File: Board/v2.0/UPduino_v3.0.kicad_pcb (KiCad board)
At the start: 4 copper layers, 62 x 22.2 mm, 116 parts, among them J1 47589-0001, J2 Right, J3 Left, J4 5V Power, U1 93LC56BT-I/OT, U2 ICE40UP5K-SG48ITR, U3 FT232H, U4 SG-210STF 12.0000ML3, U5 W25Q32JVSSIM, U6 AP2127K-3.3, U7 AP2127K-1.2, U8 SN74AUP2G125DCUR

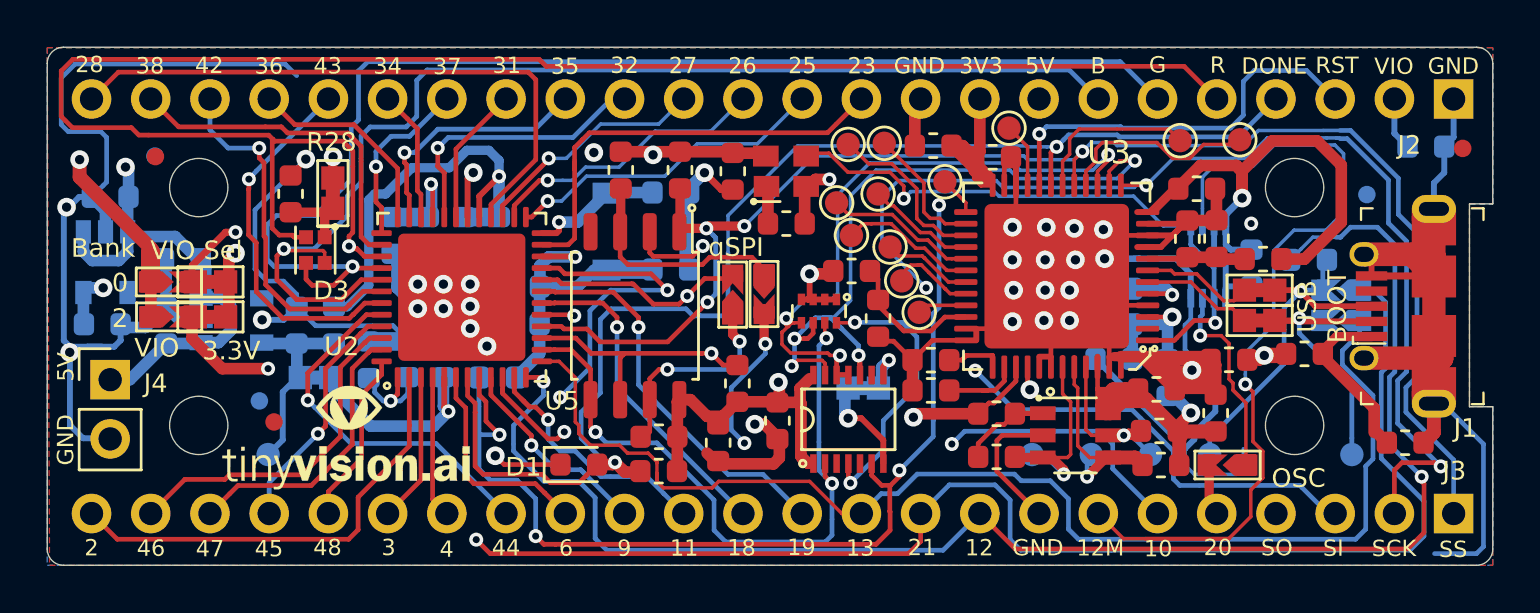
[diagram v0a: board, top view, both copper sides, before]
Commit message: Changed diode footprint, LED, modified FTDI reset, silkscreen for board and a few other changes
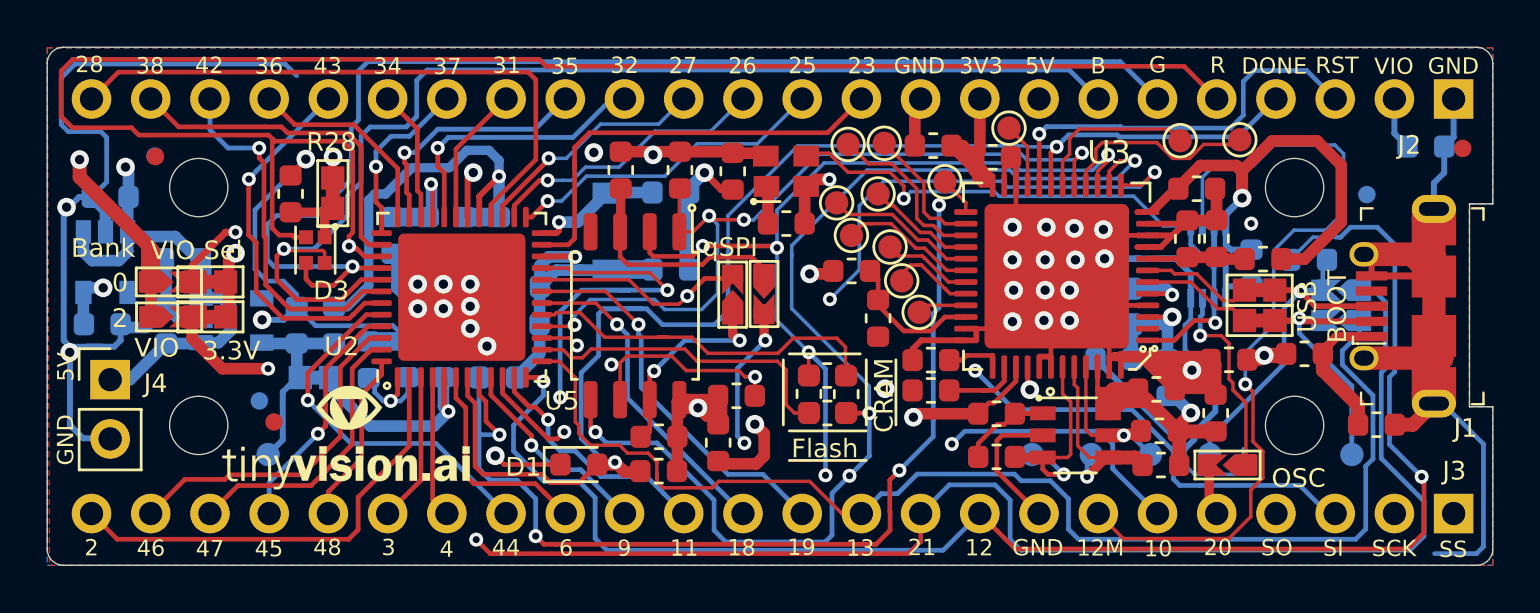
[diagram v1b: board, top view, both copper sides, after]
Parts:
- removed C32: 0.1u, Capacitor_SMD:C_0603_1608Metric
- removed RN1: YC124-JR-071KL, Resistor_SMD:R_Array_Concave_4x0402
- removed S1: TC7MPB9327FK(EL), vs:VSSOP14-P0.5-3X4
- added R11: DNI, Resistor_SMD:R_0603_1608Metric, F.Cu at (132.7, 92.7)
- added R12: 0, Resistor_SMD:R_0603_1608Metric, F.Cu at (133.5, 93.5)
- added R13: 0, Resistor_SMD:R_0603_1608Metric, F.Cu at (133.4, 91.9)
- D1: value HSMG-C120 -> LTST-C191KGKT
- R27: value JUMPER -> DNI; footprint vs:ShortedJumper-2_P1.3mm_Bridged_Pad1.0x1.0mm -> Resistor_SMD:R_0603_1608Metric; moved to F.Cu
- moved REF** 12.5 mm to (125.6, 92.5)
- moved REF** 9.26 mm to (136.5, 88.5)
- moved C25 1.45 mm to (157.0, 94.0)
- moved R27 0.77 mm to (134.3, 92.7), turned to 90 degrees
- moved R9 0.53 mm to (129.6, 92.7), turned to 180 degrees
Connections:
- R27 pad 1: GND -> /FLASH_MOSI
- R27 pad 2: Net-(R27-Pad2) -> /FPGA_SI
- R8 pad 1: /ICE_SS -> /FT_SSn
- R9 pad 1: /ICE_SCK -> /FT_SCK
- U2 pad 14: /FLASH_MOSI -> /FPGA_SO
- U2 pad 15: /ICE_SCK -> /FT_SCK
- U2 pad 16: /ICE_SS -> /FT_SSn
- U2 pad 17: /FLASH_MISO -> /FPGA_SI
- U3 pad 13: /ICE_SCK -> /FT_SCK
- U3 pad 14: /ICE_MOSI -> /FLASH_MOSI
- U3 pad 15: /ICE_MISO -> /FLASH_MISO
- U3 pad 17: /ICE_SS -> /FT_SSn
- U3 pad 39: +3V3 -> Net-(U3-Pad39)
- U5 pad 1: /ICE_SS -> /FT_SSn
- U5 pad 6: /ICE_SCK -> /FT_SCK
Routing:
- net /ICE_SCK: track 68.7 -> 0.00 mm, vias 4 -> 0
- net /ICE_SS: track 64.6 -> 0.00 mm, vias 4 -> 0
- net /FT_SCK: track 0.00 -> 36.9 mm, vias 0 -> 5
- net /FT_SSn: track 0.00 -> 34.6 mm, vias 0 -> 4
- net /ICE_MOSI: track 31.8 -> 0.00 mm, vias 4 -> 0
- net /ICE_MISO: track 28.8 -> 0.00 mm, vias 3 -> 0
- net /FLASH_MOSI: track 56.5 -> 72.8 mm, vias 4 -> 5
- net /FPGA_SI: track 0.00 -> 15.9 mm
- net +3V3: track 135.8 -> 120.2 mm
- net /FPGA_SO: track 0.00 -> 13.8 mm
- net GND: track 290.8 -> 281.5 mm
- net Net-(R27-Pad2): track 2.79 -> 0.00 mm, vias 1 -> 0
- net /IOB_18A: track 44.1 -> 41.4 mm
- net /IOB_23B: track 79.6 -> 81.6 mm
- net /CDONE: track 56.8 -> 58.7 mm
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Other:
- board text added: "CRAM"
- board text added: "Flash"

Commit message: Fixed silkscreen, removed CRAM/Flash programming switch
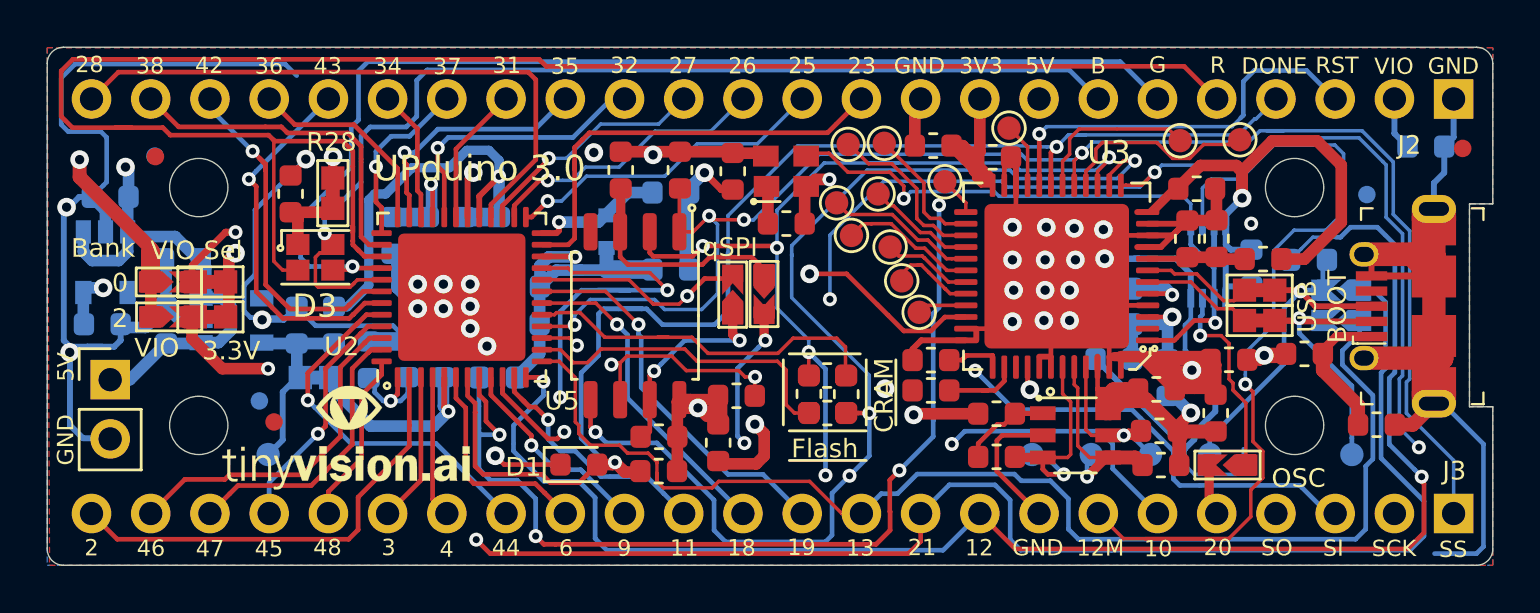
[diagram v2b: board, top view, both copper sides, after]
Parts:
- removed C26: 10n, Capacitor_SMD:C_0603_1608Metric
- removed R2: 10K, Resistor_SMD:R_0603_1608Metric
- D2: value 1N4148W-TP -> 1N4148WT-7; footprint Diode_SMD:D_SOD-123 -> Diode_SMD:D_SOD-523
- D3: value MHPA1515RGBDT-S -> CLMVC-FKA-CLBDGL7LBB79353; footprint vs:LED_1.65X1.55 -> VS.preety:LED_Cree-PLCC4_2x2mm_CW
- moved D3 0.31 mm to (111.5, 86.8), turned to 0 degrees
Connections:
- D3 pad 2: /LED_R -> /LED_B
- D3 pad 4: /LED_B -> /LED_R
- J3 pad 1: /ICE_SS -> /FT_SSn
- J3 pad 2: /ICE_SCK -> /FT_SCK
- U3 pad 34: /FT_RESET_N -> +3V3
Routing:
- net /FT_SSn: track 34.6 -> 65.9 mm
- net /FT_SCK: track 36.9 -> 64.0 mm, vias 5 -> 6
- net /FT_RESET_N: track 5.91 -> 0.00 mm
- net +3V3: track 120.2 -> 114.7 mm
- net /LED_G: track 54.0 -> 48.7 mm
- net /LED_B: track 50.1 -> 45.0 mm
- net GND: track 281.5 -> 283.3 mm
- net /LED_R: track 77.2 -> 78.4 mm, vias 1 -> 0
- net /IOB_18A: track 41.4 -> 40.5 mm
- net /CDONE: track 58.7 -> 59.5 mm
- net /CLK_12M_FT: track 26.3 -> 26.8 mm
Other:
- board text added: "UPduino 3.0"
- board text removed: "Made in USA"
